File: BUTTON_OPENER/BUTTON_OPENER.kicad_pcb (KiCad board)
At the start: 2 copper layers, 90 x 54 mm, 81 parts, among them J1 N/A, J2 OPTO_OUT_1, J3 OPTO_OUT_2, J4 OPTO_IN_1, J5 OPTO_IN_2, J6 Conn_01x05, P1 USB_C_Plug_USB2.0, Q1 BC847, Q2 BC847, Q3 BSD840N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

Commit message: Updated HW
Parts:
- removed REF**: OSHW-Symbol_8.9x8mm_SilkScreen, Symbol:OSHW-Symbol_8.9x8mm_SilkScreen
- moved R22 16.3 mm to (167.6, 81.8), turned to -90 degrees
- moved R19 14.6 mm to (165.2, 92.8), turned to 0 degrees
- moved R21 12.3 mm to (165.3, 91.2), turned to 180 degrees
- moved C2 11.5 mm to (117.8, 106.2), turned to 180 degrees
- moved R25 10.9 mm to (172.5, 91.1), turned to 180 degrees
- moved U7 10.6 mm to (172.8, 85.9)
- moved R16 10.6 mm to (150.9, 88.0), turned to 180 degrees
- moved R24 10.2 mm to (172.5, 92.6), turned to 0 degrees
- moved C13 9.01 mm to (163.0, 89.8), turned to 90 degrees
- moved U5 8.69 mm to (150.9, 82.8)
- moved R26 8.20 mm to (175.1, 82.5), turned to -90 degrees
- moved C6 7.99 mm to (165.5, 99.0), turned to -90 degrees
- moved U6 7.91 mm to (165.4, 86.0)
- moved J2 7.89 mm to (141.8, 74.8)
- moved J3 7.89 mm to (151.6, 74.8)
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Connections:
- U2 pad 26: /OPTO_IN1 -> /EN
- U2 pad 9: /EN -> /OPTO_IN1
- U4 pad 3: Net-(J2-Pin_1) -> Net-(J2-Pin_2)
- U4 pad 4: Net-(J2-Pin_2) -> Net-(J2-Pin_1)
- U5 pad 3: Net-(J3-Pin_1) -> Net-(J3-Pin_2)
- U5 pad 4: Net-(J3-Pin_2) -> Net-(J3-Pin_1)
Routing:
- net +3V3: track 12.2 -> 47.7 mm, vias 0 -> 17
- net GND: track 46.0 -> 80.2 mm, vias 6 -> 12
- net /ENC_SW: track 0.00 -> 28.3 mm
- net /VBUS: track 25.5 -> 51.1 mm, vias 2 -> 4
- net /OPTO_IN2: track 0.00 -> 21.1 mm, vias 0 -> 2
- net /OPTO_1: track 0.00 -> 20.6 mm
- net /OPTO_2: track 0.00 -> 18.1 mm, vias 0 -> 2
- net /OPTO_IN1: track 0.00 -> 17.0 mm, vias 0 -> 2
- net Net-(R7-Pad1): track 0.00 -> 12.6 mm
- net Net-(J4-Pin_1): track 0.00 -> 10.3 mm
- net Net-(J5-Pin_1): track 0.00 -> 10.1 mm
- net /B: track 14.4 -> 22.1 mm
- net Net-(J3-Pin_2): track 0.00 -> 6.68 mm
- net /R: track 18.3 -> 25.0 mm
- net Net-(C14-Pad1): track 0.00 -> 6.54 mm
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- added copper zone on B.Cu, net +3V3
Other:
- outline, holes or cut-outs redrawn

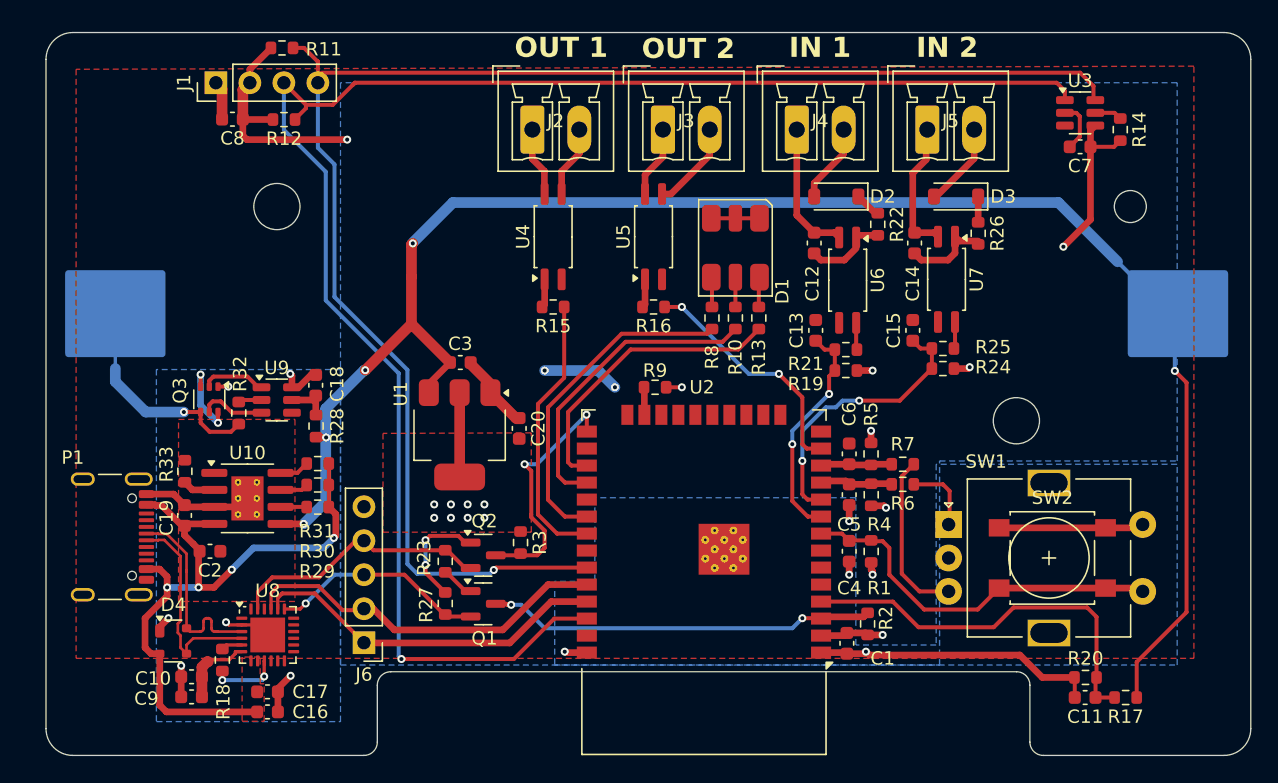
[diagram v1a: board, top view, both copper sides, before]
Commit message: Update
Connectors to screw terminals
Regulator to low dropout buck
USB C CC Resistors
IO2 pulldown resistor added
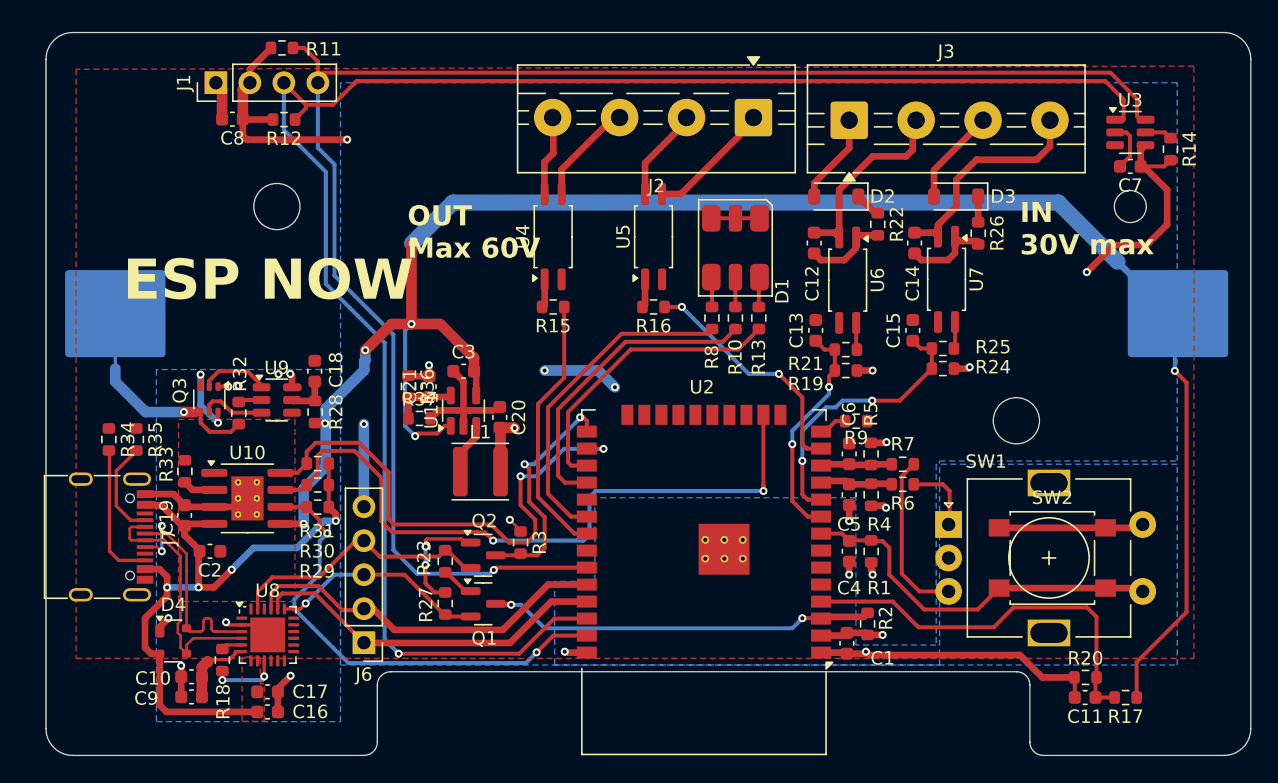
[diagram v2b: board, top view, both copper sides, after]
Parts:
- removed J4: OPTO_IN_1, Connector_Phoenix_MC:PhoenixContact_MCV_1,5_2-G-3.5_1x02_P3.50mm_Vertical
- removed J5: OPTO_IN_2, Connector_Phoenix_MC:PhoenixContact_MCV_1,5_2-G-3.5_1x02_P3.50mm_Vertical
- removed P1: USB_C_Plug_USB2.0, Connector_USB:USB_C_Receptacle_GCT_USB4105-xx-A_16P_TopMnt_Horizontal
- removed U1: N/A, Package_TO_SOT_SMD:SOT-223-3_TabPin2
- added C21: NC, Capacitor_SMD:C_0603_1608Metric, F.Cu at (134.1, 94.0)
- added J7: USB_C_Receptacle_USB2.0_14P, Connector_USB:USB_C_Receptacle_G-Switch_GT-USB-7010ASV, F.Cu at (109.2, 105.2)
- added L1: 2.2uH, Inductor_SMD:L_APV_ANR4020, F.Cu at (137.9, 100.3)
- added R34: 5.1k, Resistor_SMD:R_0603_1608Metric, F.Cu at (110.2, 97.9)
- added R35: 5.1k, Resistor_SMD:R_0603_1608Metric, F.Cu at (112.2, 97.9)
- added R36: 540K, Resistor_SMD:R_0603_1608Metric, F.Cu at (132.6, 94.0)
- added R37: 120K, Resistor_SMD:R_0603_1608Metric, F.Cu at (133.4, 96.3)
- added U11: TLV62568DBV, Package_TO_SOT_SMD:SOT-23-5, F.Cu at (136.7, 95.8)
- C20, C3: value 10uF -> 10uF 6.3V X7R
- J2: value OPTO_OUT_1 -> Screw_Terminal_01x04; footprint Connector_Phoenix_MC:PhoenixContact_MCV_1,5_2-G-3.5_1x02_P3.50mm_Vertical -> TerminalBlock:TerminalBlock_MaiXu_MX126-5.0-04P_1x04_P5.00mm
- J3: value OPTO_OUT_2 -> Screw_Terminal_01x04; footprint Connector_Phoenix_MC:PhoenixContact_MCV_1,5_2-G-3.5_1x02_P3.50mm_Vertical -> TerminalBlock:TerminalBlock_MaiXu_MX126-5.0-04P_1x04_P5.00mm
- U2: value N/A -> ESP32-WROOM
- U8: value N/A -> CP2102N
- moved J2 16.5 mm to (158.3, 73.8), turned to 180 degrees
- moved R9 15.2 mm to (166.0, 96.5), turned to 0 degrees
- moved J3 13.9 mm to (165.5, 74.0)
- moved C7 4.03 mm to (186.5, 77.5)
- moved R14 4.03 mm to (189.5, 76.2)
- moved U3 4.03 mm to (186.5, 75.0)
- moved C20 1.67 mm to (139.4, 96.2)
- moved R28 1.05 mm to (125.6, 95.8)
- moved C18 1.05 mm to (125.6, 92.8)
- moved C3 0.70 mm to (136.7, 92.8), turned to 0 degrees
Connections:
- C12 pad 2: Net-(J4-Pin_1) -> Net-(J3-Pin_2)
- C14 pad 2: Net-(J5-Pin_1) -> Net-(J3-Pin_4)
- J3 pad 1: Net-(J3-Pin_1) -> Net-(D2-A)
- R9 pad 1: +3V3 -> Net-(U2-IO12)
- R9 pad 2: Net-(U2-IO15) -> GND
- U2 pad 14: unconnected-(U2-IO12-Pad14) -> Net-(U2-IO12)
- U2 pad 16: /STDBY -> /CHRG
- U2 pad 23: Net-(U2-IO15) -> unconnected-(U2-IO15-Pad23)
- U2 pad 37: /CHRG -> /STDBY
- U4 pad 3: Net-(J2-Pin_2) -> Net-(J2-Pin_3)
- U4 pad 4: Net-(J2-Pin_1) -> Net-(J2-Pin_4)
- U5 pad 3: Net-(J3-Pin_2) -> Net-(J2-Pin_1)
- U5 pad 4: Net-(J3-Pin_1) -> Net-(J2-Pin_2)
- U6 pad 2: Net-(J4-Pin_1) -> Net-(J3-Pin_2)
- U7 pad 2: Net-(J5-Pin_1) -> Net-(J3-Pin_4)
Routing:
- net /CHRG: track 2.10 -> 51.6 mm, vias 0 -> 2
- net /EN: track 2.24 -> 39.0 mm, vias 0 -> 2
- net /STDBY: track 1.96 -> 35.6 mm, vias 0 -> 2
- net Net-(J3-Pin_4): track 0.00 -> 16.8 mm
- net /VBAT: track 126.3 -> 140.6 mm, vias 5 -> 7
- net Net-(J7-CC2): track 0.00 -> 10.3 mm
- net Net-(J4-Pin_1): track 10.3 -> 0.00 mm
- net Net-(J5-Pin_1): track 10.1 -> 0.00 mm
- net GND: track 80.2 -> 88.6 mm, vias 12 -> 15
- net Net-(J3-Pin_2): track 6.68 -> 14.6 mm
- net Net-(J2-Pin_3): track 0.00 -> 7.72 mm
- net Net-(J7-CC1): track 0.00 -> 7.26 mm
- net /SCL: track 124.1 -> 129.9 mm
- net Net-(J2-Pin_4): track 0.00 -> 5.75 mm
- net Net-(J3-Pin_1): track 5.37 -> 0.00 mm
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- removed copper zone on F.Cu, net +3V3
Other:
- board text added: "BAT+"
- board text added: "BAT-"
- board text added: "ESP NOW"
- board text added: "IN 30V max"
- board text added: "OUT Max 60V"
- board text removed: "IN 1"
- board text removed: "IN 2"
- board text removed: "OUT 1"
- board text removed: "OUT 2"

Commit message: PCB ordered with this commit
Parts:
- added H1: MountingHole, MountingHole:MountingHole_3.2mm_M3, F.Cu at (109.2, 71.2)
- added H2: MountingHole, MountingHole:MountingHole_3.2mm_M3, F.Cu at (109.2, 117.8)
- added H3: MountingHole, MountingHole:MountingHole_3.2mm_M3, F.Cu at (191.8, 71.2)
- added H4: MountingHole, MountingHole:MountingHole_3.2mm_M3, F.Cu at (191.8, 117.8)
- C1: value 10uF -> 10uF 6.3V X7R
- C10, C11, C12, C13, C14, C15, C17, C18, C19, C4, C7, C8: value 100nF -> 100nF 10V X7R
- C16, C9: value 4.7uF -> 4.7uF 10V X7R
- C2: value 1uF -> 1uF 10V X7R
- C21: value NC -> 22pF
- C5, C6: value N/A -> 100nF 10V X7R
- R10: value 1k -> 1K5
- R11, R12: value 3k3 -> 3K3
- R13, R15, R16, R21, R25, R32, R8: value 1k -> 1K
- R20: value 1k -> 8K2
- R22, R26: value 10k -> 10K
- R29, R30: value N/A -> 47K
- R31: value N/A -> 0R
- R33: value 2k2 -> 2K2
- R34, R35: value 5.1k -> 5K1
- R4, R5: value N/A -> 6K8
- R6, R7: value N/A -> 1K
- U11: value TLV62568DBV -> SUNTEK SK6615CS5
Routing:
- net +3V3: track 53.0 -> 53.5 mm, vias 11 -> 12
- added copper zone on F.Cu, net +3V3
